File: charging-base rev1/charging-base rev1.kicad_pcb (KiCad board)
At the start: 2 copper layers, 85 x 85 mm, 0 parts

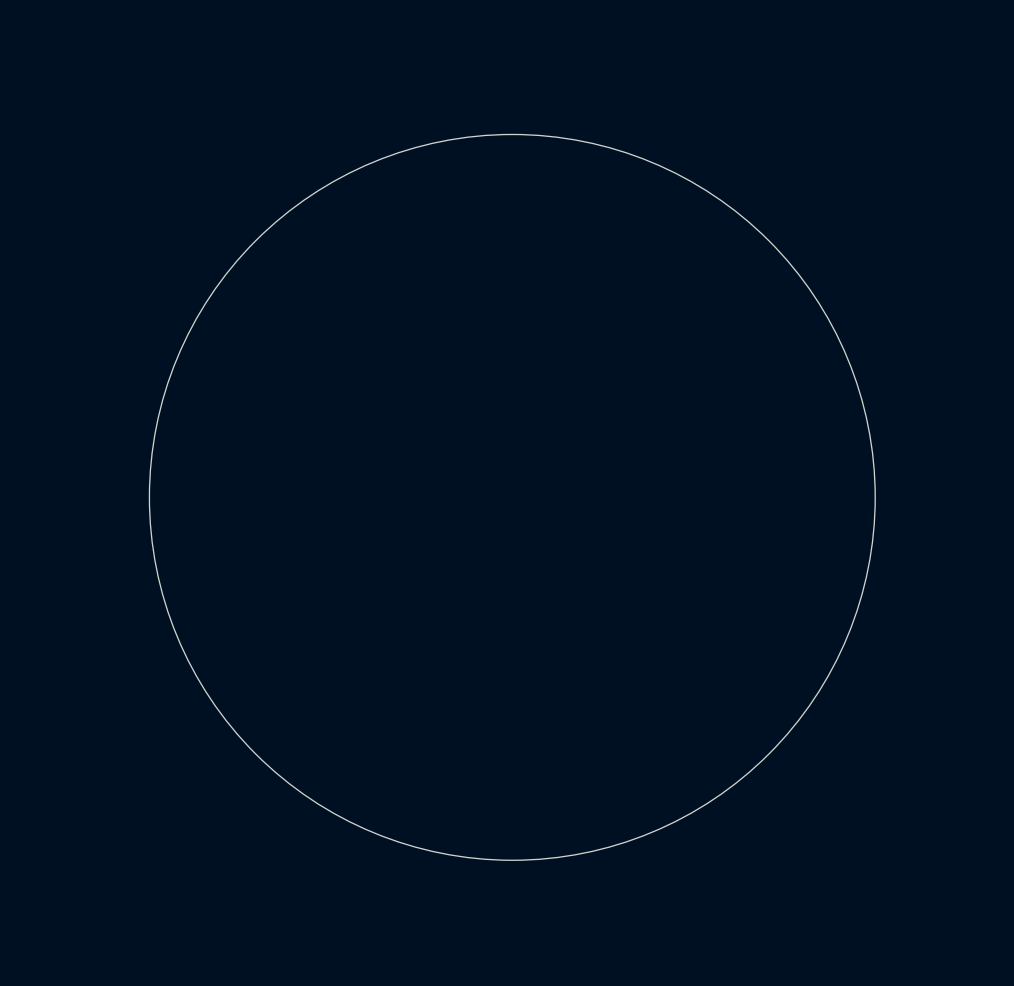
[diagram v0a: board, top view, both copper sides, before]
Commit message: finished rev1 of layout, resistor sensor not yet selected
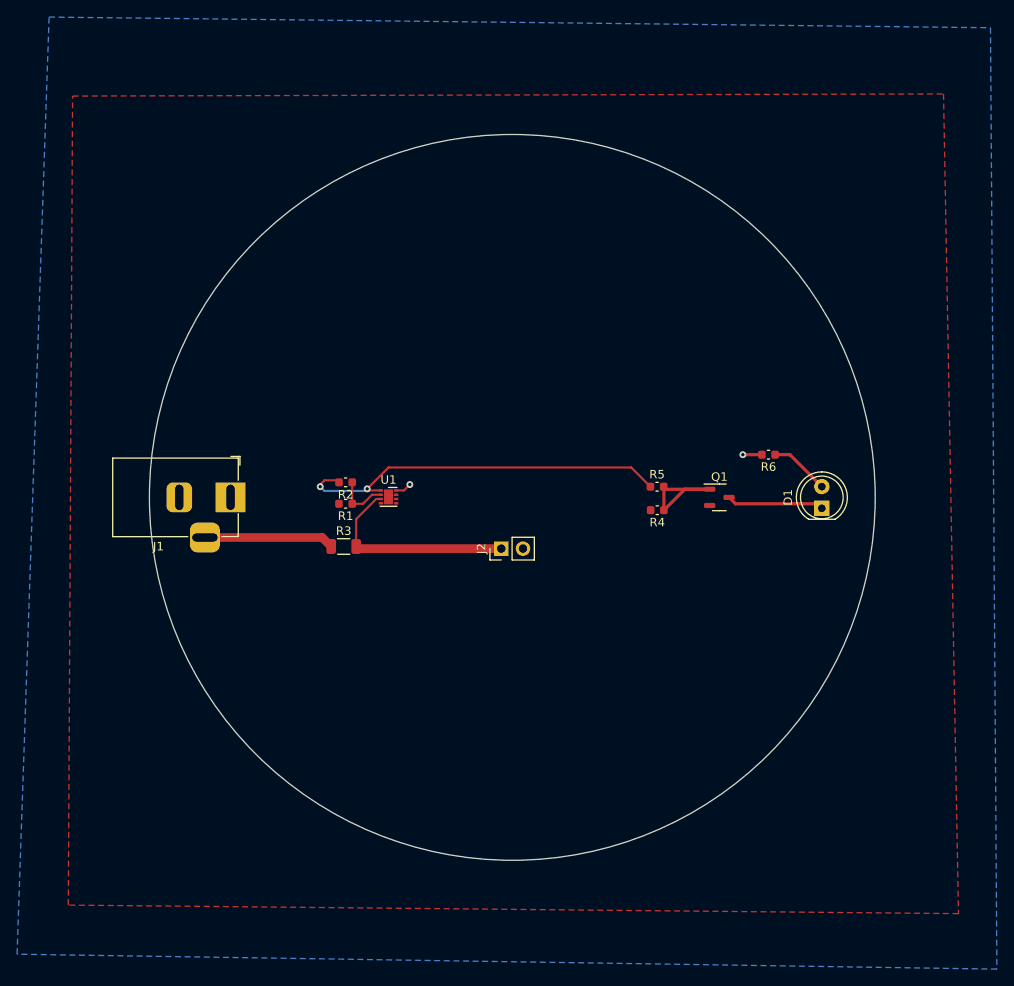
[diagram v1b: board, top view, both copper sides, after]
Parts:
- added D1: LED, LED_THT:LED_D5.0mm, F.Cu at (186.2, 101.3)
- added J1: Barrel_Jack, Connector_BarrelJack:BarrelJack_Horizontal, F.Cu at (117.0, 100.0)
- added J2: PowerToDino, Connector_PinHeader_2.54mm:PinHeader_1x02_P2.54mm_Vertical, F.Cu at (148.7, 106.0)
- added Q1: NMOS, Package_TO_SOT_SMD:SOT-23-3, F.Cu at (174.2, 100.0)
- added R1: R, Capacitor_SMD:C_0603_1608Metric, F.Cu at (130.5, 100.8)
- added R2: R, Capacitor_SMD:C_0603_1608Metric, F.Cu at (130.5, 98.2)
- added R3: 250mOhm, Resistor_SMD:R_1206_3216Metric, F.Cu at (130.2, 105.8)
- added R4: 10K, Capacitor_SMD:C_0603_1608Metric, F.Cu at (167.0, 101.5)
- added R5: 10, Capacitor_SMD:C_0603_1608Metric, F.Cu at (166.9, 98.8)
- added R6: 220, Capacitor_SMD:C_0603_1608Metric, F.Cu at (180.0, 95.0)
- added U1: LM358_DFN, Package_DFN_QFN:DFN-8-1EP_2x2mm_P0.5mm_EP1.05x1.75mm, F.Cu at (135.5, 99.9)
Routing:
- net /output-voltage: track 0.00 -> 45.4 mm, vias 0 -> 2
- net Net-(J2-Pin_1): track 0.00 -> 24.2 mm
- net GND: track 0.00 -> 15.2 mm
- net Net-(Q1-G): track 0.00 -> 14.6 mm
- net Net-(D1-K): track 0.00 -> 11.4 mm
- net Net-(D1-A): track 0.00 -> 7.02 mm
- net Net-(U1A--): track 0.00 -> 6.30 mm
- net +VDC: track 0.00 -> 4.11 mm, vias 0 -> 2
- added copper zone on B.Cu, net +VDC
- added copper zone on F.Cu, net GND

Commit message: added barrel plug source, changed footprint U1
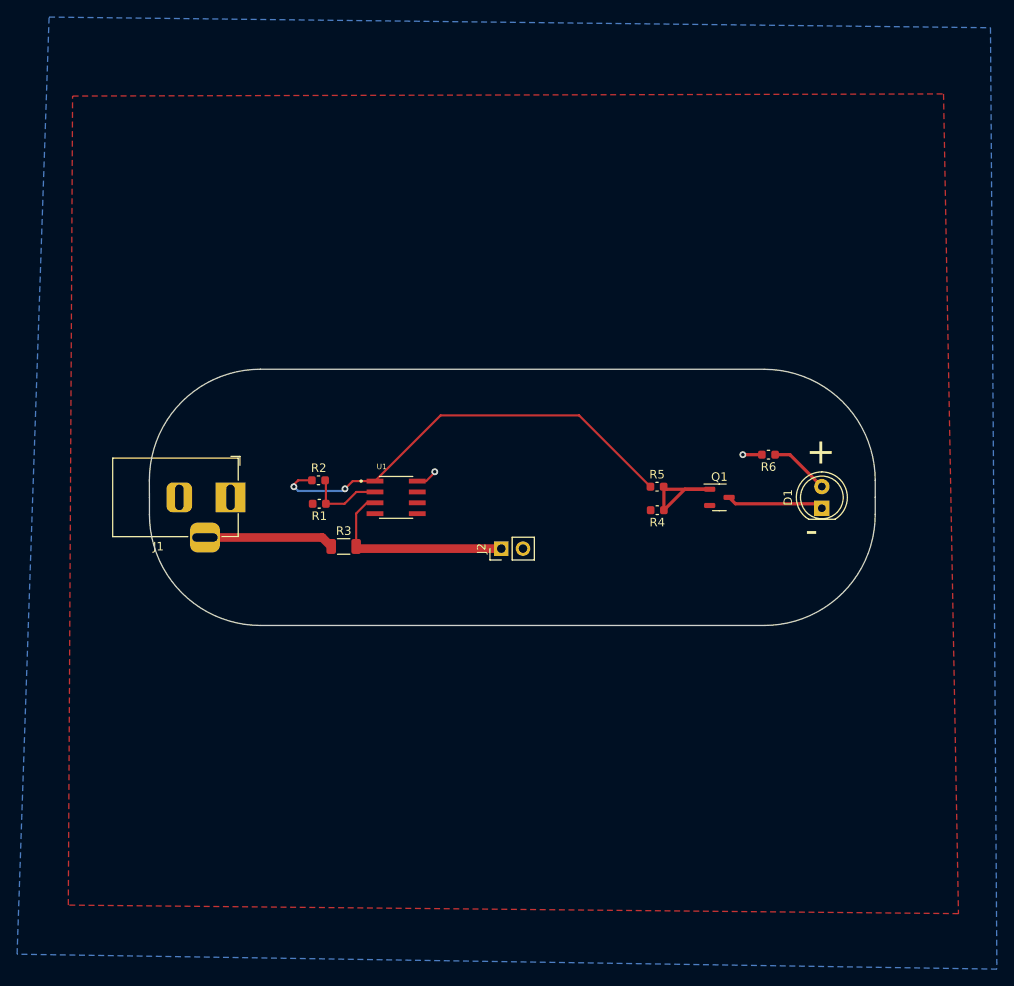
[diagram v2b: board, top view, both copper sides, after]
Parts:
- R1: value R -> 10K
- R2: value R -> 1M
- U1: footprint Package_DFN_QFN:DFN-8-1EP_2x2mm_P0.5mm_EP1.05x1.75mm -> LM358DT:SOIC127P600X175-8N
- moved R2 3.18 mm to (127.3, 98.0)
- moved R1 3.08 mm to (127.4, 100.8)
- moved U1 0.89 mm to (136.4, 100.0)
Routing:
- net /output-voltage: track 45.4 -> 51.4 mm
- net Net-(U1A--): track 6.30 -> 9.11 mm
- net +VDC: track 4.11 -> 4.78 mm
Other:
- board size 85 x 85 mm -> 85 x 30 mm
- board text added: "+"
- board text added: "-"
